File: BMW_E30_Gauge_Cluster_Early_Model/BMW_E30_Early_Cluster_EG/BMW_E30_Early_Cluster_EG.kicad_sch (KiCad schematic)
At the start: 0 parts

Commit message: Started Tach and EG Schematics
Started pinouts for tachometer and EG schematics. Also made a notation update to the Nexus schematic, removed a TODO that was completed.
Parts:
- added J1: Conn_01x05_Pin, symbol Connector:Conn_01x05_Pin
- added R1: R, symbol Device:R
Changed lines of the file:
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@@
 		(title "BMW E30 Gauge Cluster Economy Gauge")
+	)
+	(symbol
+		(lib_id "Connector:Conn_01x05_Pin")
+		(at 46.99 67.31 0)
+		(unit 1)
+		(exclude_from_sim no)
+		(in_bom yes)
+		(on_board yes)
+		(dnp no)
+		(property "Reference" "J1"
+			(at 52.324 58.42 0)
+			(effects
+				(font
+					(size 1.27 1.27)
+				)
+			)
+		)
+		(property "Value" "Conn_01x05_Pin"
+			(at 47.625 59.69 0)
+			(effects
+				(font
+					(size 1.27 1.27)
+				)
+				(hide yes)
+			)
+		)
+		(property "Footprint" ""
+			(at 46.99 67.31 0)
+			(effects
+				(font
+					(size 1.27 1.27)
+				)
+				(hide yes)
+			)
+		)
+		(property "Datasheet" "~"
+			(at 46.99 67.31 0)
+			(effects
+				(font
+					(size 1.27 1.27)
+				)
+				(hide yes)
+			)
+		)
+		(property "Description" "Generic connector, single row, 01x05, script generated"
+			(at 46.99 67.31 0)
+			(effects
+				(font
+					(size 1.27 1.27)
+				)
+				(hide yes)
+			)
+		)
+		(pin "5"
+		)
+		(pin "3"
+		)
+		(pin "2"
+		)
+		(pin "1"
+		)
+		(pin "4"
+		)
+		(instances
+			(project ""
+				(path "/87822f16-f981-4ad2-bfeb-178300c0bdac"
+					(reference "J1")
+					(unit 1)
+				)
+			)
+		)
+	)
+	(symbol
+		(lib_id "Device:R")
+		(at 87.63 57.15 0)
+		(unit 1)
+		(exclude_from_sim no)
+		(in_bom yes)
+		(on_board yes)
+		(dnp no)
+		(fields_autoplaced yes)
+		(property "Reference" "R1"
+			(at 90.17 55.8799 0)
+			(effects
+				(font
+					(size 1.27 1.27)
+				)
+				(justify left)
+			)
+		)
+		(property "Value" "R"
+			(at 90.17 58.4199 0)
+			(effects
+				(font
+					(size 1.27 1.27)
+				)
+				(justify left)
+			)
+		)
+		(property "Footprint" ""
+			(at 85.852 57.15 90)
+			(effects
+				(font
+					(size 1.27 1.27)
+				)
+				(hide yes)
+			)
+		)
+		(property "Datasheet" "~"
+			(at 87.63 57.15 0)
+			(effects
+				(font
+					(size 1.27 1.27)
+				)
+				(hide yes)
+			)
+		)
+		(property "Description" "Resistor"
+			(at 87.63 57.15 0)
+			(effects
+				(font
+					(size 1.27 1.27)
+				)
+				(hide yes)
+			)
+		)
+		(pin "2"
+		)
+		(pin "1"
+		)
+		(instances
+			(project ""
+				(path "/87822f16-f981-4ad2-bfeb-178300c0bdac"
+					(reference "R1")
+					(unit 1)
+				)
+			)
+		)
 	)
 	(sheet_instances

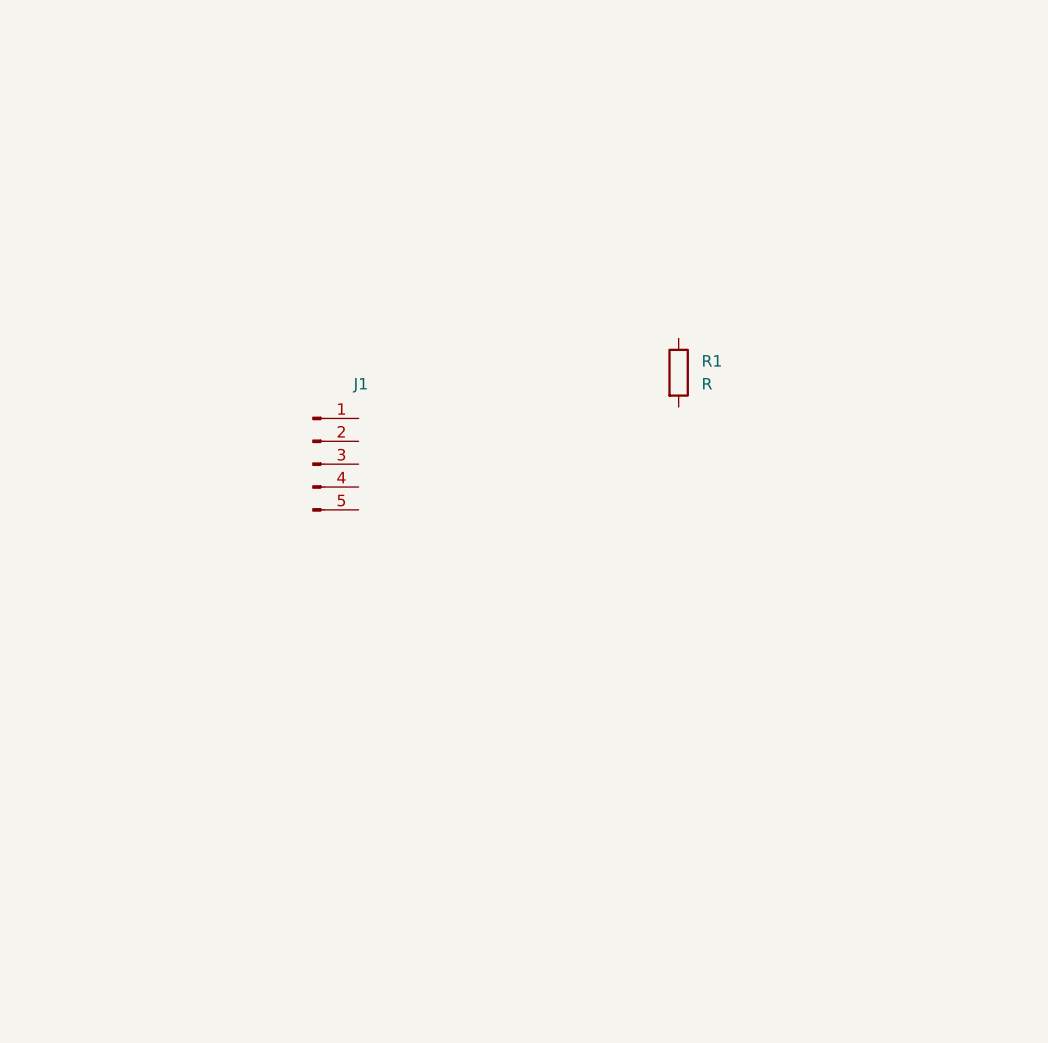
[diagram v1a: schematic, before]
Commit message: Tachometer Schematic Completed
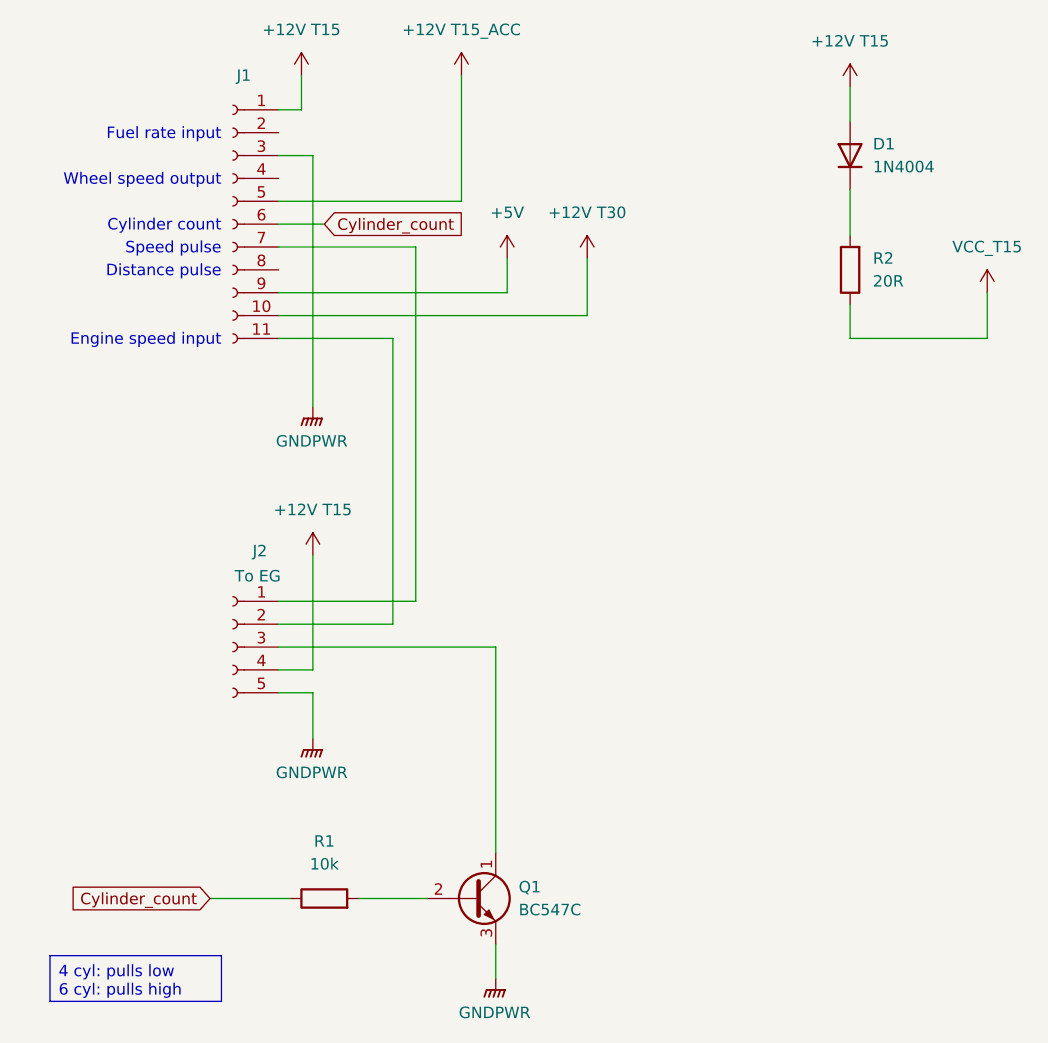
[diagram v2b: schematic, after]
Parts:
- removed J1: Conn_01x05_Pin, symbol Connector:Conn_01x05_Pin
- added D1: 1N4004, Diode_THT:D_DO-41_SOD81_P10.16mm_Horizontal, symbol Diode:1N4005
- added J1: Conn_01x11_Socket, symbol Connector:Conn_01x11_Socket
- added J2: To EG, symbol Connector:Conn_01x05_Socket
- added Q1: BC547C, Package_TO_SOT_THT:TO-92_Inline, symbol Transistor_BJT:BC547
- added R2: 20R, symbol Device:R
- R1: value R -> 10k
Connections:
- net Cylinder_count: now reaches R1.1
- net Cylinder_count: now also J1.6 (Pin_6)
- net at R1.2: now also Q1.2 (B)
- new net: J1.11 (Pin_11), J2.2 (Pin_2)
- new net: J1.7 (Pin_7), J2.1 (Pin_1)
- new net: D1.1 (K), R2.2
- new net: J2.3 (Pin_3), Q1.1 (C)
- new net +12V T15: D1.2 (A), J1.1 (Pin_1), J2.4 (Pin_4)
- new net +12V T15_ACC: J1.5 (Pin_5)
- new net +12V T30: J1.10 (Pin_10)
- new net +5V: J1.9 (Pin_9)
- new net GNDPWR: J1.3 (Pin_3), J2.5 (Pin_5), Q1.3 (E)
- new net VCC_T15: R2.1
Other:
- note added: "Cylinder count"
- note added: "Distance pulse"
- note added: "Engine speed input"
- note added: "Fuel rate input"
- note added: "Speed pulse"
- note added: "Wheel speed output"
- company: (none) -> Reagan Ansel
- title: BMW E30 Gauge Cluster Economy Gauge -> BMW E30 Gauge Cluster Fuel Economy Gauge

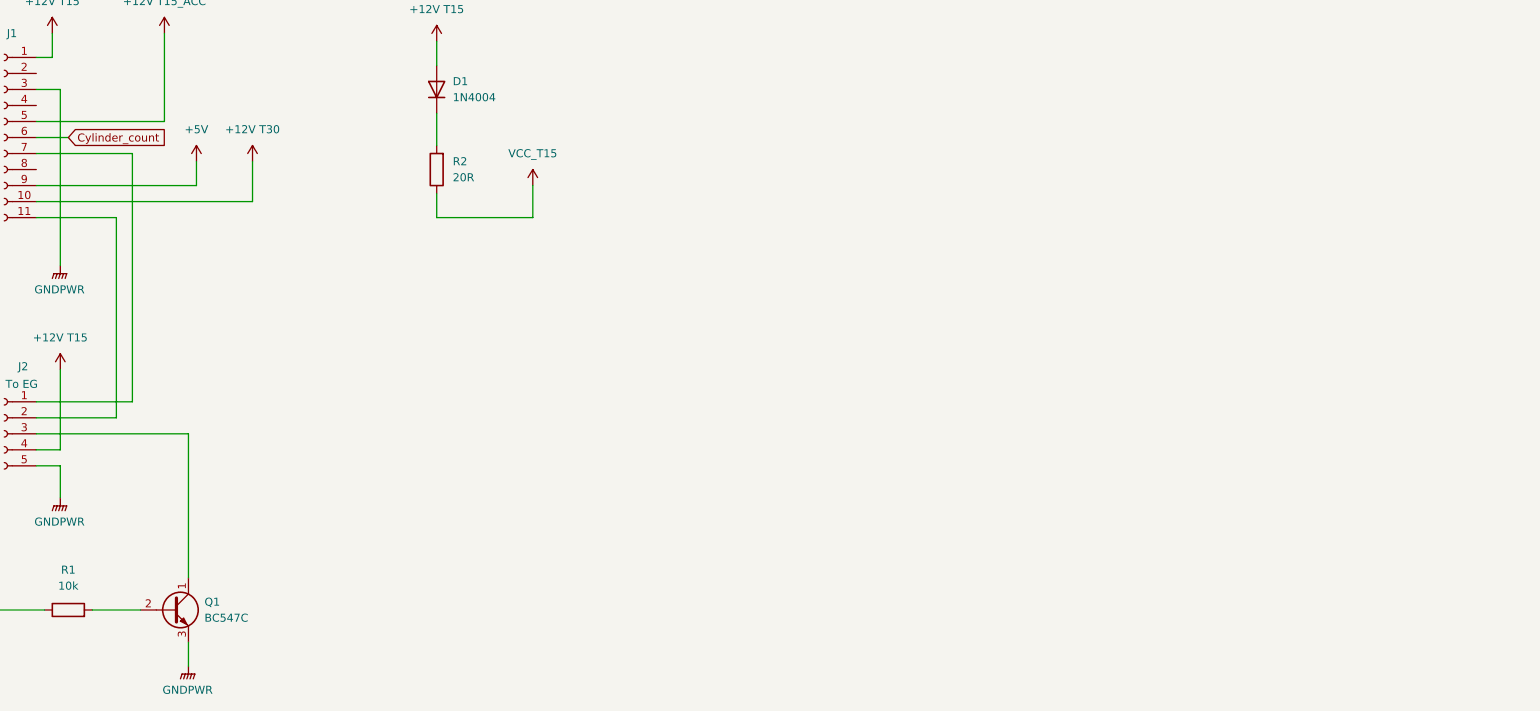
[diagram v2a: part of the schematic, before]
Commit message: Added Datasheets
Datasheets for the chips on the EG board.
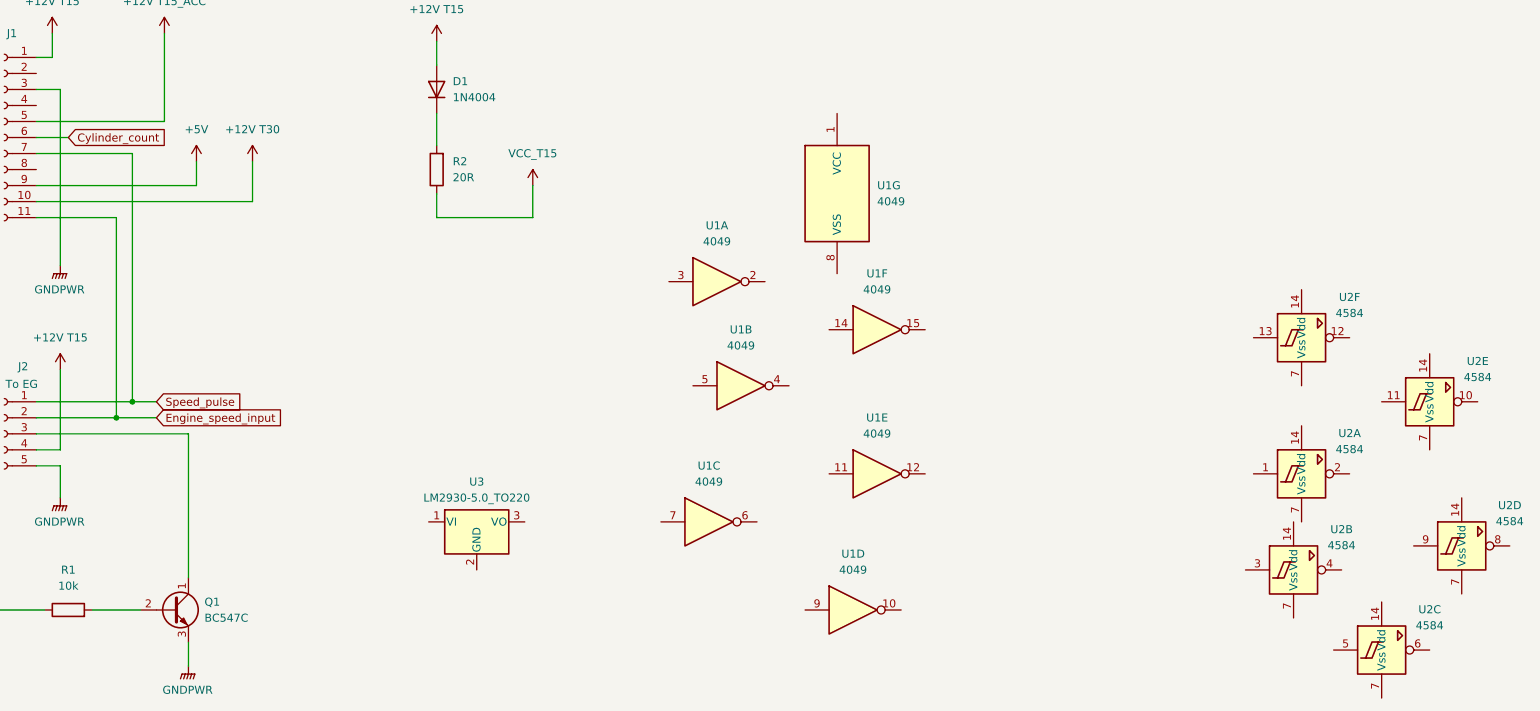
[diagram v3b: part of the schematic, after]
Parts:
- added U1: 4049, Package_DIP:DIP-14_W7.62mm_Socket, symbol 4xxx:4049
- added U2: 4584, symbol 4xxx_IEEE:4584
- added U3: LM2930-5.0_TO220, Package_TO_SOT_THT:TO-220-3_Vertical, symbol Regulator_Linear:LM2931-5.0_TO220
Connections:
- net Engine_speed_input: now reaches J1.11 (Pin_11), J2.2 (Pin_2)
- net Speed_pulse: now reaches J1.7 (Pin_7), J2.1 (Pin_1)

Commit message: EG Schematic Updates
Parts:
- added C1: 47u, symbol Device:C_Polarized
- added C2: 33n, symbol Device:C
- added C3: 47n, symbol Device:C
- added C4: ?, symbol Device:C
- added D2, D3: 1N1418, Diode_THT:D_DO-34_SOD68_P10.16mm_Horizontal, symbol Diode:1N4005
- added MES1: Fuel Economy Gauge, symbol Device:Galvanometer
- added Q2: BC337, Package_TO_SOT_THT:TO-92_Inline, symbol Transistor_BJT:BC337
- added R10: 803R 1%, Resistor_THT:R_Axial_DIN0207_L6.3mm_D2.5mm_P10.16mm_Horizontal, symbol Device:R
- added R11, R14, R4: 47k, Resistor_THT:R_Axial_DIN0207_L6.3mm_D2.5mm_P10.16mm_Horizontal, symbol Device:R
- added R12, R13, R3: 10k, Resistor_THT:R_Axial_DIN0207_L6.3mm_D2.5mm_P10.16mm_Horizontal, symbol Device:R
- added R15: 120R, Resistor_THT:R_Axial_DIN0207_L6.3mm_D2.5mm_P10.16mm_Horizontal, symbol Device:R
- added R5: 16k, Resistor_THT:R_Axial_DIN0207_L6.3mm_D2.5mm_P10.16mm_Horizontal, symbol Device:R
- added R6: 39k, Resistor_THT:R_Axial_DIN0207_L6.3mm_D2.5mm_P10.16mm_Horizontal, symbol Device:R
- added R7: 33k, Resistor_THT:R_Axial_DIN0207_L6.3mm_D2.5mm_P10.16mm_Horizontal, symbol Device:R
- added R8: 100k, Resistor_THT:R_Axial_DIN0207_L6.3mm_D2.5mm_P10.16mm_Horizontal, symbol Device:R
- added R9: 36k, Resistor_THT:R_Axial_DIN0207_L6.3mm_D2.5mm_P10.16mm_Horizontal, symbol Device:R
- added U4: LM2903, Package_DIP:DIP-8_W7.62mm_Socket, symbol Comparator:LM2903
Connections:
- net +5V: now also U2.14 (Vdd), U2.14 (Vdd), U2.14 (Vdd), U2.14 (Vdd), U2.14 (Vdd), U2.14 (Vdd), U3.3 (VO), C1.1
- net GNDPWR: now also U2.7 (Vss), U2.7 (Vss), U2.7 (Vss), U2.7 (Vss), U2.7 (Vss), U2.7 (Vss), U3.2 (GND), C1.2, C2.2, C3.2, R10.2, R11.2, R15.2, R7.2, U4.4 (V-)
- net VCC_T15: now also U3.1 (VI), C2.1, C4.1, MES1.2 (+), R13.1, R14.1, R3.2, R5.2, R6.2, U4.8 (V+)
- net Fuel_rate_input: now reaches J1.2 (Pin_2)
- net Fuel_rate_input: now also D2.1 (K)
- net Wheel_speed_output: now reaches J1.4 (Pin_4)
- net Wheel_speed_output: now also D3.1 (K)
- net PIC_P11: now reaches J1.8 (Pin_8)
- net 4527_P9: now reaches U2.12
- net at U2.13: now also R10.1, R11.1, R9.1
- net PIC_P7: now reaches U2.10
- net at U2.11: now also R12.1
- net ~{6_cyl}: now reaches J2.3 (Pin_3), Q1.1 (C)
- net Cylinder_count renamed 6_cyl
- new net: D2.2 (A), R3.1, R4.2
- new net: C4.2, MES1.1 (-), Q2.1 (C)
- new net: C3.1, Q2.2 (B), R14.2, U4.7
- new net: Q2.3 (E), R15.1, U4.6 (-)
- new net: R6.1, R7.1, R8.2, U4.3 (+)
- new net: D3.2 (A), R5.1, R9.2
- new net: R12.2, R13.2, R8.1, U4.1
- new net: R4.1, U4.2 (-)
- no-connect marks 0 -> 3
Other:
- moved on the sheet: U1A, U1B, U1C, U1D, U1E, U1F, U1G, U2A, U2B, U2C, U2D, U2E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

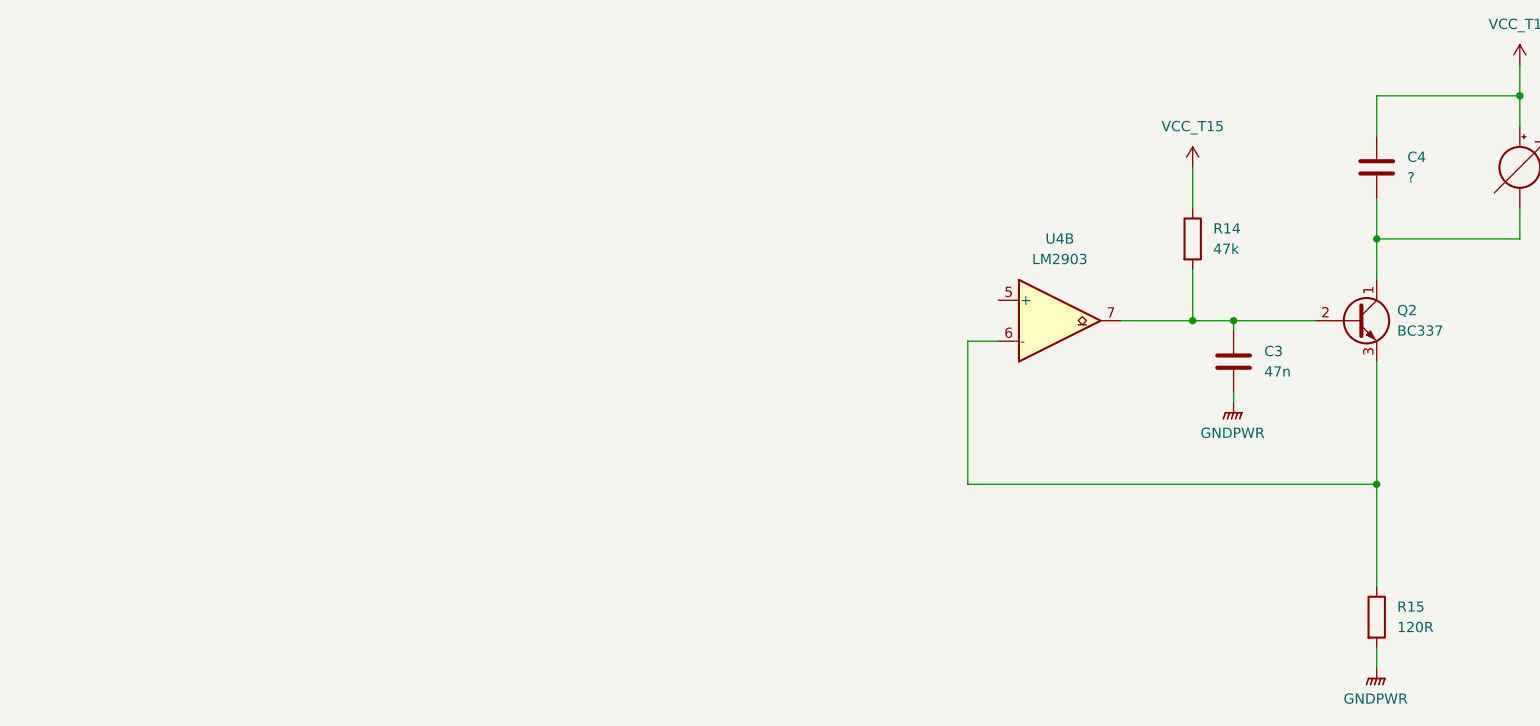
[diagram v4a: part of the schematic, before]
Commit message: EG Schematic Updates
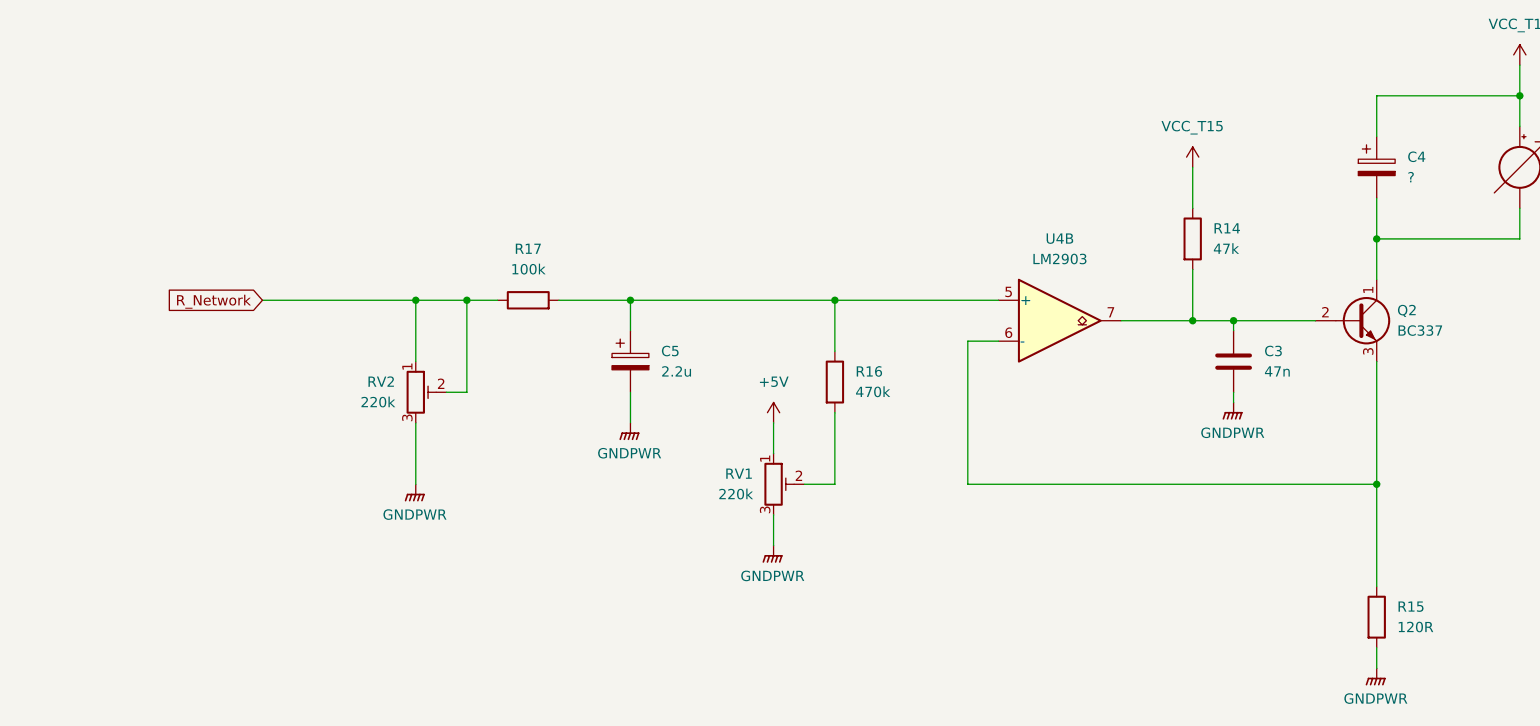
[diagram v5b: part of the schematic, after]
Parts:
- added C5: 2.2u, symbol Device:C_Polarized
- added R16: 470k, Resistor_THT:R_Axial_DIN0207_L6.3mm_D2.5mm_P10.16mm_Horizontal, symbol Device:R
- added R17: 100k, Resistor_THT:R_Axial_DIN0207_L6.3mm_D2.5mm_P10.16mm_Horizontal, symbol Device:R
- added RV1, RV2: 220k, symbol Device:R_Potentiometer_Trim
- C4: symbol Device:C -> Device:C_Polarized
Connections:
- net +5V: now also RV1.1
- net GNDPWR: now also C5.2, RV1.3, RV2.3
- net at U4.5 (+): now also C5.1, R16.1, R17.2
- new net: R16.2, RV1.2
- new net R_Network: R17.1, RV2.1, RV2.2

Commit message: Updates to EG Schematic
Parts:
- added C6: 100u, symbol Device:C_Polarized
- added D4: 1N1418, Diode_THT:D_DO-34_SOD68_P10.16mm_Horizontal, symbol Diode:1N4005
- added D5: BZX55C 18V, symbol Device:D_Zener
- added R18: 2k7, Resistor_THT:R_Axial_DIN0207_L6.3mm_D2.5mm_P10.16mm_Horizontal, symbol Device:R
- added RN1: R2R_8B, Resistor_THT:R_Array_SIP8, symbol BMW_ICs:R2R_8B
- added U5: SAJ300R, symbol BMW_ICs:SAJ300R
- added Y1: 160 kHz, symbol Device:Crystal
- U1: footprint Package_DIP:DIP-14_W7.62mm_Socket -> Package_DIP:DIP-16_W7.62mm
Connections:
- net +5V: now also U1.1 (VCC), D4.1 (K)
- net GNDPWR: now also U1.8 (VSS), U2.9, C6.2, D5.2 (A), RN1.8 (R7), U5.13 (GND)
- net PIC_P11: now also U1.14
- net VCC_T15: now also C6.1, R18.2
- net at U2.5: now also U5.8 (M)
- net PIC_P27: now reaches U2.6
- net at C4.2, MES1.1 (-), Q2.1 (C): now also D5.1 (K)
- net at U1.15: now also RN1.7 (R6)
- net at U1.6: now also RN1.3 (R2)
- net PIC_P15: now reaches U1.7
- net at U1.10: now also RN1.2 (R1)
- net PIC_P16: now reaches U1.9
- net PIC_P14: now reaches U1.11
- net at U1.12: now also RN1.4 (R3)
- net at U1.4: now also RN1.5 (R4)
- net PIC_P13: now reaches U1.5
- net at U1.2: now also RN1.6 (R5)
- net PIC_P12: now reaches U1.3
- net R_Network: no longer names the net of R17.1, RV2.1, RV2.2
- net R_Network: now also RN1.1 (Bit_out)
- new net: D4.2 (A), R18.1, U5.14 (VCC)
- new net: U5.10 (CLK), Y1.1
- new net: U5.9 (CLK), Y1.2
- no-connect marks 3 -> 14
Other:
- moved on the sheet: C3, C4, C5, MES1, Q2, R14, R15, R16, R17, RV1, RV2, U1A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
